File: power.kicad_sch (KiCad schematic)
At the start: 0 parts

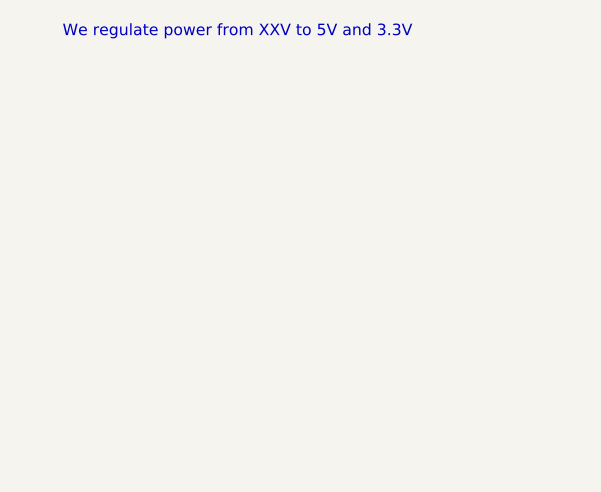
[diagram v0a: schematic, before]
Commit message: Add voltage reference and voltage regulator
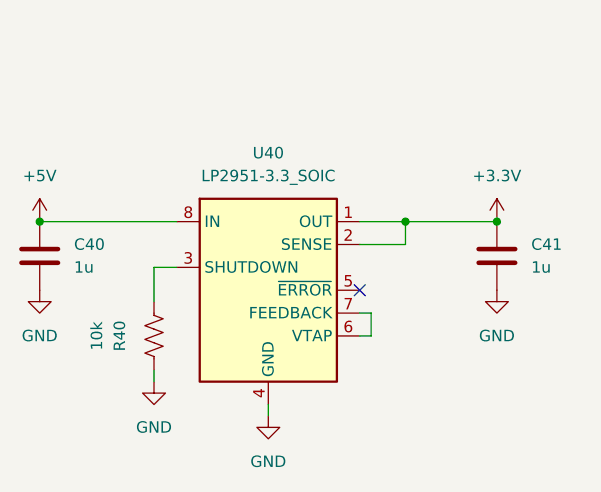
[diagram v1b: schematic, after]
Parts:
- added C40, C41: 1u, Capacitor_SMD:C_0805_2012Metric, symbol Device:C
- added R40: 10k, Resistor_SMD:R_0805_2012Metric, symbol Device:R_US
- added U40: LP2951-3.3_SOIC, Package_SO:SOIC-8_3.9x4.9mm_P1.27mm, symbol Regulator_Linear:LP2951-3.3_SOIC
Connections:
- new net: R40.1, U40.3 (SHUTDOWN)
- new net: U40.6 (VTAP), U40.7 (FEEDBACK)
- new net +3V3: C41.1, U40.1 (OUT), U40.2 (SENSE)
- new net +5V: C40.1, U40.8 (IN)
- new net GND: C40.2, C41.2, R40.2, U40.4 (GND)
- no-connect marks 0 -> 1
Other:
- note removed: "We regulate power from XXV to 5V and 3.3V"
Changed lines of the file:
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@@
 (kicad_sch (version 20211123) (generator eeschema)
   (paper "A4")
-  (text "We regulate power from XXV to 5V and 3.3V" (at 132.08 43.18 0)
-    (effects (font (size 1.27 1.27)) (justify left bottom))
+  (junction (at 129.54 63.5) (diameter 0) (color 0 0 0 0)
+  )
+  (junction (at 170.18 63.5) (diameter 0) (color 0 0 0 0)
+  )
+  (junction (at 180.34 63.5) (diameter 0) (color 0 0 0 0)
+  )
+  (no_connect (at 165.1 71.12))
+  (wire (pts (xy 142.24 68.58) (xy 144.78 68.58))
+    (stroke (width 0) (type default) (color 0 0 0 0))
+  )
+  (wire (pts (xy 165.1 63.5) (xy 170.18 63.5))
+    (stroke (width 0) (type default) (color 0 0 0 0))
+  )
+  (wire (pts (xy 170.18 63.5) (xy 170.18 66.04))
+    (stroke (width 0) (type default) (color 0 0 0 0))
+  )
+  (wire (pts (xy 166.37 73.66) (xy 165.1 73.66))
+    (stroke (width 0) (type default) (color 0 0 0 0))
+  )
+  (wire (pts (xy 129.54 63.5) (xy 144.78 63.5))
+    (stroke (width 0) (type default) (color 0 0 0 0))
+  )
+  (wire (pts (xy 166.37 76.2) (xy 165.1 76.2))
+    (stroke (width 0) (type default) (color 0 0 0 0))
+  )
+  (wire (pts (xy 170.18 66.04) (xy 165.1 66.04))
+    (stroke (width 0) (type default) (color 0 0 0 0))
+  )
+  (wire (pts (xy 142.24 72.39) (xy 142.24 68.58))
+    (stroke (width 0) (type default) (color 0 0 0 0))
+  )
+  (wire (pts (xy 154.94 83.82) (xy 154.94 85.09))
+    (stroke (width 0) (type default) (color 0 0 0 0))
+  )
+  (wire (pts (xy 180.34 63.5) (xy 170.18 63.5))
+    (stroke (width 0) (type default) (color 0 0 0 0))
+  )
+  (wire (pts (xy 166.37 73.66) (xy 166.37 76.2))
+    (stroke (width 0) (type default) (color 0 0 0 0))
+  )
+  (wire (pts (xy 142.24 80.01) (xy 142.24 81.28))
+    (stroke (width 0) (type default) (color 0 0 0 0))
+  )
+  (symbol (lib_id "power:GND") (at 154.94 85.09 0) (unit 1)
+    (in_bom yes) (on_board yes) (fields_autoplaced)
+    (property "Reference" "#PWR0122" (id 0) (at 154.94 91.44 0)
+      (effects (font (size 1.27 1.27)) hide)
+    )
+    (property "Value" "GND" (id 1) (at 154.94 90.17 0))
+    (property "Footprint" "" (id 2) (at 154.94 85.09 0)
+      (effects (font (size 1.27 1.27)) hide)
+    )
+    (property "Datasheet" "" (id 3) (at 154.94 85.09 0)
+      (effects (font (size 1.27 1.27)) hide)
+    )
+    (pin "1")
+  )
+  (symbol (lib_id "power:+3.3V") (at 180.34 63.5 0) (unit 1)
+    (in_bom yes) (on_board yes) (fields_autoplaced)
+    (property "Reference" "#PWR0126" (id 0) (at 180.34 67.31 0)
+      (effects (font (size 1.27 1.27)) hide)
+    )
+    (property "Value" "+3.3V" (id 1) (at 180.34 58.42 0))
+    (property "Footprint" "" (id 2) (at 180.34 63.5 0)
+      (effects (font (size 1.27 1.27)) hide)
+    )
+    (property "Datasheet" "" (id 3) (at 180.34 63.5 0)
+      (effects (font (size 1.27 1.27)) hide)
+    )
+    (pin "1")
+  )
+  (symbol (lib_id "Device:C") (at 180.34 67.31 0) (unit 1)
+    (in_bom yes) (on_board yes) (fields_autoplaced)
+    (property "Reference" "C41" (id 0) (at 184.15 66.0399 0)
+      (effects (font (size 1.27 1.27)) (justify left))
+    )
+    (property "Value" "1u" (id 1) (at 184.15 68.5799 0)
+      (effects (font (size 1.27 1.27)) (justify left))
+    )
+    (property "Footprint" "Capacitor_SMD:C_0805_2012Metric" (id 2) (at 181.3052 71.12 0)
+      (effects (font (size 1.27 1.27)) hide)
+    )
+    (property "Datasheet" "~" (id 3) (at 180.34 67.31 0)
+      (effects (font (size 1.27 1.27)) hide)
+    )
+    (pin "1")
+    (pin "2")
+  )
+  (symbol (lib_id "power:GND") (at 129.54 71.12 0) (unit 1)
+    (in_bom yes) (on_board yes) (fields_autoplaced)
+    (property "Reference" "#PWR0123" (id 0) (at 129.54 77.47 0)
+      (effects (font (size 1.27 1.27)) hide)
+    )
+    (property "Value" "GND" (id 1) (at 129.54 76.2 0))
+    (property "Footprint" "" (id 2) (at 129.54 71.12 0)
+      (effects (font (size 1.27 1.27)) hide)
+    )
+    (property "Datasheet" "" (id 3) (at 129.54 71.12 0)
+      (effects (font (size 1.27 1.27)) hide)
+    )
+    (pin "1")
+  )
+  (symbol (lib_id "power:GND") (at 142.24 81.28 0) (unit 1)
+    (in_bom yes) (on_board yes) (fields_autoplaced)
+    (property "Reference" "#PWR0121" (id 0) (at 142.24 87.63 0)
+      (effects (font (size 1.27 1.27)) hide)
+    )
+    (property "Value" "GND" (id 1) (at 142.24 86.36 0))
+    (property "Footprint" "" (id 2) (at 142.24 81.28 0)
+      (effects (font (size 1.27 1.27)) hide)
+    )
+    (property "Datasheet" "" (id 3) (at 142.24 81.28 0)
+      (effects (font (size 1.27 1.27)) hide)
+    )
+    (pin "1")
+  )
+  (symbol (lib_id "power:+5V") (at 129.54 63.5 0) (unit 1)
+    (in_bom yes) (on_board yes) (fields_autoplaced)
+    (property "Reference" "#PWR0124" (id 0) (at 129.54 67.31 0)
+      (effects (font (size 1.27 1.27)) hide)
+    )
+    (property "Value" "+5V" (id 1) (at 129.54 58.42 0))
+    (property "Footprint" "" (id 2) (at 129.54 63.5 0)
+      (effects (font (size 1.27 1.27)) hide)
+    )
+    (property "Datasheet" "" (id 3) (at 129.54 63.5 0)
+      (effects (font (size 1.27 1.27)) hide)
+    )
+    (pin "1")
+  )
+  (symbol (lib_id "Device:C") (at 129.54 67.31 0) (unit 1)
+    (in_bom yes) (on_board yes) (fields_autoplaced)
+    (property "Reference" "C40" (id 0) (at 133.35 66.0399 0)
+      (effects (font (size 1.27 1.27)) (justify left))
+    )
+    (property "Value" "1u" (id 1) (at 133.35 68.5799 0)
+      (effects (font (size 1.27 1.27)) (justify left))
+    )
+    (property "Footprint" "Capacitor_SMD:C_0805_2012Metric" (id 2) (at 130.5052 71.12 0)
+      (effects (font (size 1.27 1.27)) hide)
+    )
+    (property "Datasheet" "~" (id 3) (at 129.54 67.31 0)
+      (effects (font (size 1.27 1.27)) hide)
+    )
+    (pin "1")
+    (pin "2")
+  )
+  (symbol (lib_id "Regulator_Linear:LP2951-3.3_SOIC") (at 154.94 71.12 0) (unit 1)
+    (in_bom yes) (on_board yes) (fields_autoplaced)
+    (property "Reference" "U40" (id 0) (at 154.94 55.88 0))
+    (property "Value" "LP2951-3.3_SOIC" (id 1) (at 154.94 58.42 0))
+    (property "Footprint" "Package_SO:SOIC-8_3.9x4.9mm_P1.27mm" (id 2) (at 154.94 87.63 0)
+      (effects (font (size 1.27 1.27)) hide)
+    )
+    (property "Datasheet" "http://www.ti.com/lit/ds/symlink/lp2951.pdf" (id 3) (at 154.94 71.12 0)
+      (effects (font (size 1.27 1.27)) hide)
+    )
+    (pin "1")
+    (pin "2")
+    (pin "3")
+    (pin "4")
+    (pin "5")
+    (pin "6")
+    (pin "7")
+    (pin "8")
+  )
+  (symbol (lib_id "power:GND") (at 180.34 71.12 0) (unit 1)
+    (in_bom yes) (on_board yes) (fields_autoplaced)
+    (property "Reference" "#PWR0125" (id 0) (at 180.34 77.47 0)
+      (effects (font (size 1.27 1.27)) hide)
+    )
+    (property "Value" "GND" (id 1) (at 180.34 76.2 0))
+    (property "Footprint" "" (id 2) (at 180.34 71.12 0)
+      (effects (font (size 1.27 1.27)) hide)
+    )
+    (property "Datasheet" "" (id 3) (at 180.34 71.12 0)
+      (effects (font (size 1.27 1.27)) hide)
+    )
+    (pin "1")
+  )
+  (symbol (lib_id "Device:R_US") (at 142.24 76.2 0) (unit 1)
+    (in_bom yes) (on_board yes)
+    (property "Reference" "R40" (id 0) (at 138.43 76.2 90))
+    (property "Value" "10k" (id 1) (at 135.89 76.2 90))
+    (property "Footprint" "Resistor_SMD:R_0805_2012Metric" (id 2) (at 143.256 76.454 90)
+      (effects (font (size 1.27 1.27)) hide)
+    )
+    (property "Datasheet" "~" (id 3) (at 142.24 76.2 0)
+      (effects (font (size 1.27 1.27)) hide)
+    )
+    (pin "1")
+    (pin "2")
   )
 )

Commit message: WIP PCB Routing
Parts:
- C40, C41: value 1u -> (none); footprint Capacitor_SMD:C_0805_2012Metric -> (none)
- R40: value 10k -> (none); footprint Resistor_SMD:R_0805_2012Metric -> (none)
- U40: value LP2951-3.3_SOIC -> (none); footprint Package_SO:SOIC-8_3.9x4.9mm_P1.27mm -> (none)
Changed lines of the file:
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@@
       (effects (font (size 1.27 1.27)) (justify left))
     )
-    (property "Value" "1u" (id 1) (at 184.15 68.5799 0)
+    (property "Value" "" (id 1) (at 184.15 68.5799 0)
       (effects (font (size 1.27 1.27)) (justify left))
     )
-    (property "Footprint" "Capacitor_SMD:C_0805_2012Metric" (id 2) (at 181.3052 71.12 0)
+    (property "Footprint" "" (id 2) (at 181.3052 71.12 0)
       (effects (font (size 1.27 1.27)) hide)
     )
@@
       (effects (font (size 1.27 1.27)) (justify left))
     )
-    (property "Value" "1u" (id 1) (at 133.35 68.5799 0)
+    (property "Value" "" (id 1) (at 133.35 68.5799 0)
       (effects (font (size 1.27 1.27)) (justify left))
     )
-    (property "Footprint" "Capacitor_SMD:C_0805_2012Metric" (id 2) (at 130.5052 71.12 0)
+    (property "Footprint" "" (id 2) (at 130.5052 71.12 0)
       (effects (font (size 1.27 1.27)) hide)
     )
@@
     (in_bom yes) (on_board yes) (fields_autoplaced)
     (property "Reference" "U40" (id 0) (at 154.94 55.88 0))
-    (property "Value" "LP2951-3.3_SOIC" (id 1) (at 154.94 58.42 0))
-    (property "Footprint" "Package_SO:SOIC-8_3.9x4.9mm_P1.27mm" (id 2) (at 154.94 87.63 0)
+    (property "Value" "" (id 1) (at 154.94 58.42 0))
+    (property "Footprint" "" (id 2) (at 154.94 87.63 0)
       (effects (font (size 1.27 1.27)) hide)
     )
@@
     (in_bom yes) (on_board yes)
     (property "Reference" "R40" (id 0) (at 138.43 76.2 90))
-    (property "Value" "10k" (id 1) (at 135.89 76.2 90))
-    (property "Footprint" "Resistor_SMD:R_0805_2012Metric" (id 2) (at 143.256 76.454 90)
+    (property "Value" "" (id 1) (at 135.89 76.2 90))
+    (property "Footprint" "" (id 2) (at 143.256 76.454 90)
       (effects (font (size 1.27 1.27)) hide)
     )

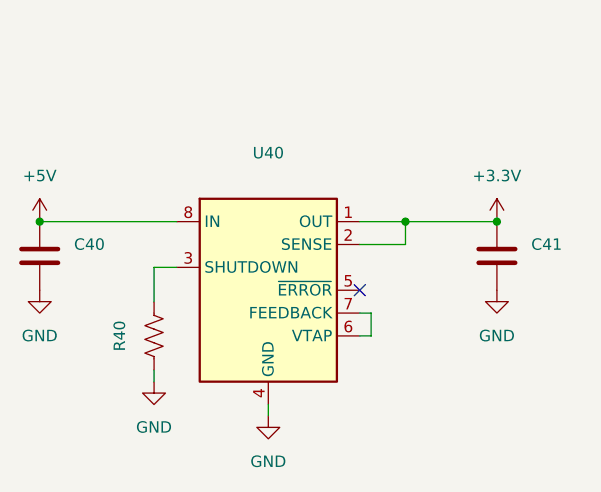
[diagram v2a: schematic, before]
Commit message: Add heatsink, among other things
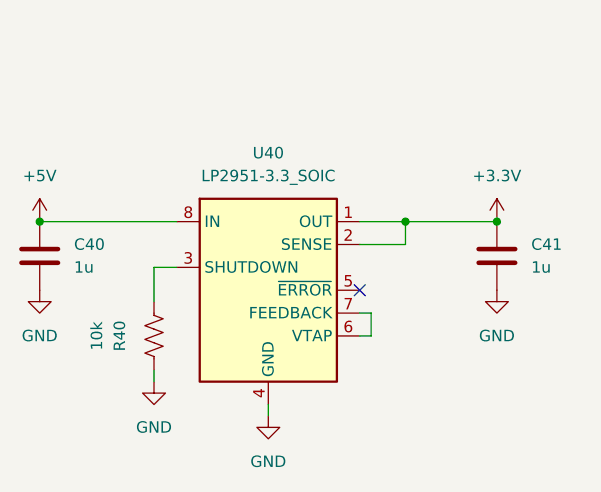
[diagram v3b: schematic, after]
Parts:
- C40, C41: value (none) -> 1u; footprint (none) -> Capacitor_SMD:C_0805_2012Metric
- R40: value (none) -> 10k; footprint (none) -> Resistor_SMD:R_0805_2012Metric
- U40: value (none) -> LP2951-3.3_SOIC; footprint (none) -> Package_SO:SOIC-8_3.9x4.9mm_P1.27mm
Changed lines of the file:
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@@
       (effects (font (size 1.27 1.27)) (justify left))
     )
-    (property "Value" "" (id 1) (at 184.15 68.5799 0)
+    (property "Value" "1u" (id 1) (at 184.15 68.5799 0)
       (effects (font (size 1.27 1.27)) (justify left))
     )
-    (property "Footprint" "" (id 2) (at 181.3052 71.12 0)
+    (property "Footprint" "Capacitor_SMD:C_0805_2012Metric" (id 2) (at 181.3052 71.12 0)
       (effects (font (size 1.27 1.27)) hide)
     )
@@
       (effects (font (size 1.27 1.27)) (justify left))
     )
-    (property "Value" "" (id 1) (at 133.35 68.5799 0)
+    (property "Value" "1u" (id 1) (at 133.35 68.5799 0)
       (effects (font (size 1.27 1.27)) (justify left))
     )
-    (property "Footprint" "" (id 2) (at 130.5052 71.12 0)
+    (property "Footprint" "Capacitor_SMD:C_0805_2012Metric" (id 2) (at 130.5052 71.12 0)
       (effects (font (size 1.27 1.27)) hide)
     )
@@
     (in_bom yes) (on_board yes) (fields_autoplaced)
     (property "Reference" "U40" (id 0) (at 154.94 55.88 0))
-    (property "Value" "" (id 1) (at 154.94 58.42 0))
-    (property "Footprint" "" (id 2) (at 154.94 87.63 0)
+    (property "Value" "LP2951-3.3_SOIC" (id 1) (at 154.94 58.42 0))
+    (property "Footprint" "Package_SO:SOIC-8_3.9x4.9mm_P1.27mm" (id 2) (at 154.94 87.63 0)
       (effects (font (size 1.27 1.27)) hide)
     )
@@
     (in_bom yes) (on_board yes)
     (property "Reference" "R40" (id 0) (at 138.43 76.2 90))
-    (property "Value" "" (id 1) (at 135.89 76.2 90))
-    (property "Footprint" "" (id 2) (at 143.256 76.454 90)
+    (property "Value" "10k" (id 1) (at 135.89 76.2 90))
+    (property "Footprint" "Resistor_SMD:R_0805_2012Metric" (id 2) (at 143.256 76.454 90)
       (effects (font (size 1.27 1.27)) hide)
     )

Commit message: WIP routing
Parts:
- C701: renamed from C40; value 1u -> (none); footprint Capacitor_SMD:C_0805_2012Metric -> (none)
- C702: renamed from C41; value 1u -> (none); footprint Capacitor_SMD:C_0805_2012Metric -> (none)
- R701: renamed from R40; value 10k -> (none); footprint Resistor_SMD:R_0805_2012Metric -> (none)
- U701: renamed from U40; value LP2951-3.3_SOIC -> (none); footprint Package_SO:SOIC-8_3.9x4.9mm_P1.27mm -> (none)
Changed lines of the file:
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@@
   (symbol (lib_id "power:GND") (at 154.94 85.09 0) (unit 1)
     (in_bom yes) (on_board yes) (fields_autoplaced)
-    (property "Reference" "#PWR0122" (id 0) (at 154.94 91.44 0)
+    (property "Reference" "#PWR0704" (id 0) (at 154.94 91.44 0)
       (effects (font (size 1.27 1.27)) hide)
     )
@@
   (symbol (lib_id "power:+3.3V") (at 180.34 63.5 0) (unit 1)
     (in_bom yes) (on_board yes) (fields_autoplaced)
-    (property "Reference" "#PWR0126" (id 0) (at 180.34 67.31 0)
+    (property "Reference" "#PWR0705" (id 0) (at 180.34 67.31 0)
       (effects (font (size 1.27 1.27)) hide)
     )
@@
   (symbol (lib_id "Device:C") (at 180.34 67.31 0) (unit 1)
     (in_bom yes) (on_board yes) (fields_autoplaced)
-    (property "Reference" "C41" (id 0) (at 184.15 66.0399 0)
+    (property "Reference" "C702" (id 0) (at 184.15 66.0399 0)
       (effects (font (size 1.27 1.27)) (justify left))
     )
-    (property "Value" "1u" (id 1) (at 184.15 68.5799 0)
+    (property "Value" "" (id 1) (at 184.15 68.5799 0)
       (effects (font (size 1.27 1.27)) (justify left))
     )
-    (property "Footprint" "Capacitor_SMD:C_0805_2012Metric" (id 2) (at 181.3052 71.12 0)
+    (property "Footprint" "" (id 2) (at 181.3052 71.12 0)
       (effects (font (size 1.27 1.27)) hide)
     )
@@
   (symbol (lib_id "power:GND") (at 129.54 71.12 0) (unit 1)
     (in_bom yes) (on_board yes) (fields_autoplaced)
-    (property "Reference" "#PWR0123" (id 0) (at 129.54 77.47 0)
+    (property "Reference" "#PWR0702" (id 0) (at 129.54 77.47 0)
       (effects (font (size 1.27 1.27)) hide)
     )
@@
   (symbol (lib_id "power:GND") (at 142.24 81.28 0) (unit 1)
     (in_bom yes) (on_board yes) (fields_autoplaced)
-    (property "Reference" "#PWR0121" (id 0) (at 142.24 87.63 0)
+    (property "Reference" "#PWR0703" (id 0) (at 142.24 87.63 0)
       (effects (font (size 1.27 1.27)) hide)
     )
@@
   (symbol (lib_id "power:+5V") (at 129.54 63.5 0) (unit 1)
     (in_bom yes) (on_board yes) (fields_autoplaced)
-    (property "Reference" "#PWR0124" (id 0) (at 129.54 67.31 0)
+    (property "Reference" "#PWR0701" (id 0) (at 129.54 67.31 0)
       (effects (font (size 1.27 1.27)) hide)
     )
@@
   (symbol (lib_id "Device:C") (at 129.54 67.31 0) (unit 1)
     (in_bom yes) (on_board yes) (fields_autoplaced)
-    (property "Reference" "C40" (id 0) (at 133.35 66.0399 0)
+    (property "Reference" "C701" (id 0) (at 133.35 66.0399 0)
       (effects (font (size 1.27 1.27)) (justify left))
     )
-    (property "Value" "1u" (id 1) (at 133.35 68.5799 0)
+    (property "Value" "" (id 1) (at 133.35 68.5799 0)
       (effects (font (size 1.27 1.27)) (justify left))
     )
-    (property "Footprint" "Capacitor_SMD:C_0805_2012Metric" (id 2) (at 130.5052 71.12 0)
+    (property "Footprint" "" (id 2) (at 130.5052 71.12 0)
       (effects (font (size 1.27 1.27)) hide)
     )
@@
   (symbol (lib_id "Regulator_Linear:LP2951-3.3_SOIC") (at 154.94 71.12 0) (unit 1)
     (in_bom yes) (on_board yes) (fields_autoplaced)
-    (property "Reference" "U40" (id 0) (at 154.94 55.88 0))
-    (property "Value" "LP2951-3.3_SOIC" (id 1) (at 154.94 58.42 0))
-    (property "Footprint" "Package_SO:SOIC-8_3.9x4.9mm_P1.27mm" (id 2) (at 154.94 87.63 0)
+    (property "Reference" "U701" (id 0) (at 154.94 55.88 0))
+    (property "Value" "" (id 1) (at 154.94 58.42 0))
+    (property "Footprint" "" (id 2) (at 154.94 87.63 0)
       (effects (font (size 1.27 1.27)) hide)
     )
@@
   (symbol (lib_id "power:GND") (at 180.34 71.12 0) (unit 1)
     (in_bom yes) (on_board yes) (fields_autoplaced)
-    (property "Reference" "#PWR0125" (id 0) (at 180.34 77.47 0)
+    (property "Reference" "#PWR0706" (id 0) (at 180.34 77.47 0)
       (effects (font (size 1.27 1.27)) hide)
     )
@@
   (symbol (lib_id "Device:R_US") (at 142.24 76.2 0) (unit 1)
     (in_bom yes) (on_board yes)
-    (property "Reference" "R40" (id 0) (at 138.43 76.2 90))
-    (property "Value" "10k" (id 1) (at 135.89 76.2 90))
-    (property "Footprint" "Resistor_SMD:R_0805_2012Metric" (id 2) (at 143.256 76.454 90)
+    (property "Reference" "R701" (id 0) (at 138.43 76.2 90))
+    (property "Value" "" (id 1) (at 135.89 76.2 90))
+    (property "Footprint" "" (id 2) (at 143.256 76.454 90)
       (effects (font (size 1.27 1.27)) hide)
     )

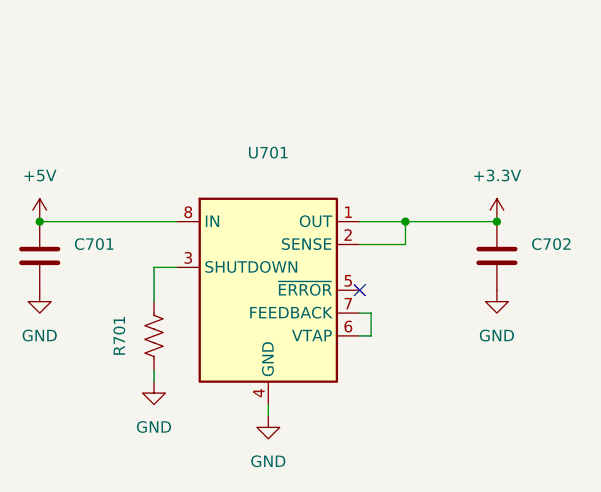
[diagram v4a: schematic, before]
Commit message: Fix and tune differential pair and zones
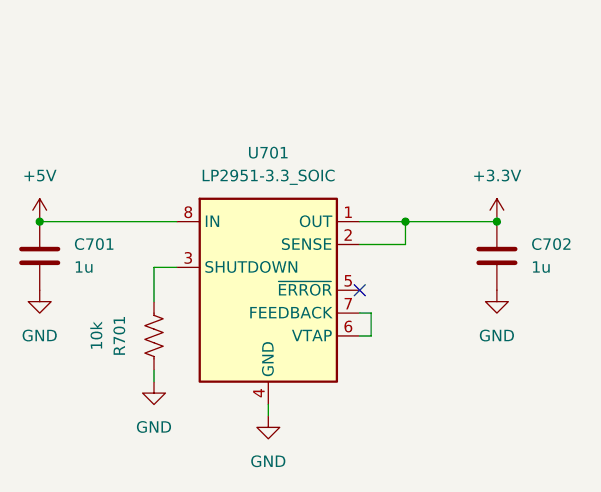
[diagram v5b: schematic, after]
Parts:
- C701, C702: value (none) -> 1u; footprint (none) -> Capacitor_SMD:C_0805_2012Metric
- R701: value (none) -> 10k; footprint (none) -> Resistor_SMD:R_0805_2012Metric
- U701: value (none) -> LP2951-3.3_SOIC; footprint (none) -> Package_SO:SOIC-8_3.9x4.9mm_P1.27mm
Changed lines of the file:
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@@
       (effects (font (size 1.27 1.27)) (justify left))
     )
-    (property "Value" "" (id 1) (at 184.15 68.5799 0)
+    (property "Value" "1u" (id 1) (at 184.15 68.5799 0)
       (effects (font (size 1.27 1.27)) (justify left))
     )
-    (property "Footprint" "" (id 2) (at 181.3052 71.12 0)
+    (property "Footprint" "Capacitor_SMD:C_0805_2012Metric" (id 2) (at 181.3052 71.12 0)
       (effects (font (size 1.27 1.27)) hide)
     )
@@
       (effects (font (size 1.27 1.27)) (justify left))
     )
-    (property "Value" "" (id 1) (at 133.35 68.5799 0)
+    (property "Value" "1u" (id 1) (at 133.35 68.5799 0)
       (effects (font (size 1.27 1.27)) (justify left))
     )
-    (property "Footprint" "" (id 2) (at 130.5052 71.12 0)
+    (property "Footprint" "Capacitor_SMD:C_0805_2012Metric" (id 2) (at 130.5052 71.12 0)
       (effects (font (size 1.27 1.27)) hide)
     )
@@
     (in_bom yes) (on_board yes) (fields_autoplaced)
     (property "Reference" "U701" (id 0) (at 154.94 55.88 0))
-    (property "Value" "" (id 1) (at 154.94 58.42 0))
-    (property "Footprint" "" (id 2) (at 154.94 87.63 0)
+    (property "Value" "LP2951-3.3_SOIC" (id 1) (at 154.94 58.42 0))
+    (property "Footprint" "Package_SO:SOIC-8_3.9x4.9mm_P1.27mm" (id 2) (at 154.94 87.63 0)
       (effects (font (size 1.27 1.27)) hide)
     )
@@
     (in_bom yes) (on_board yes)
     (property "Reference" "R701" (id 0) (at 138.43 76.2 90))
-    (property "Value" "" (id 1) (at 135.89 76.2 90))
-    (property "Footprint" "" (id 2) (at 143.256 76.454 90)
+    (property "Value" "10k" (id 1) (at 135.89 76.2 90))
+    (property "Footprint" "Resistor_SMD:R_0805_2012Metric" (id 2) (at 143.256 76.454 90)
       (effects (font (size 1.27 1.27)) hide)
     )
